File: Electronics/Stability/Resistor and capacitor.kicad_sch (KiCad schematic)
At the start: 5 parts, among them U1 ${SIM.PARAMS}

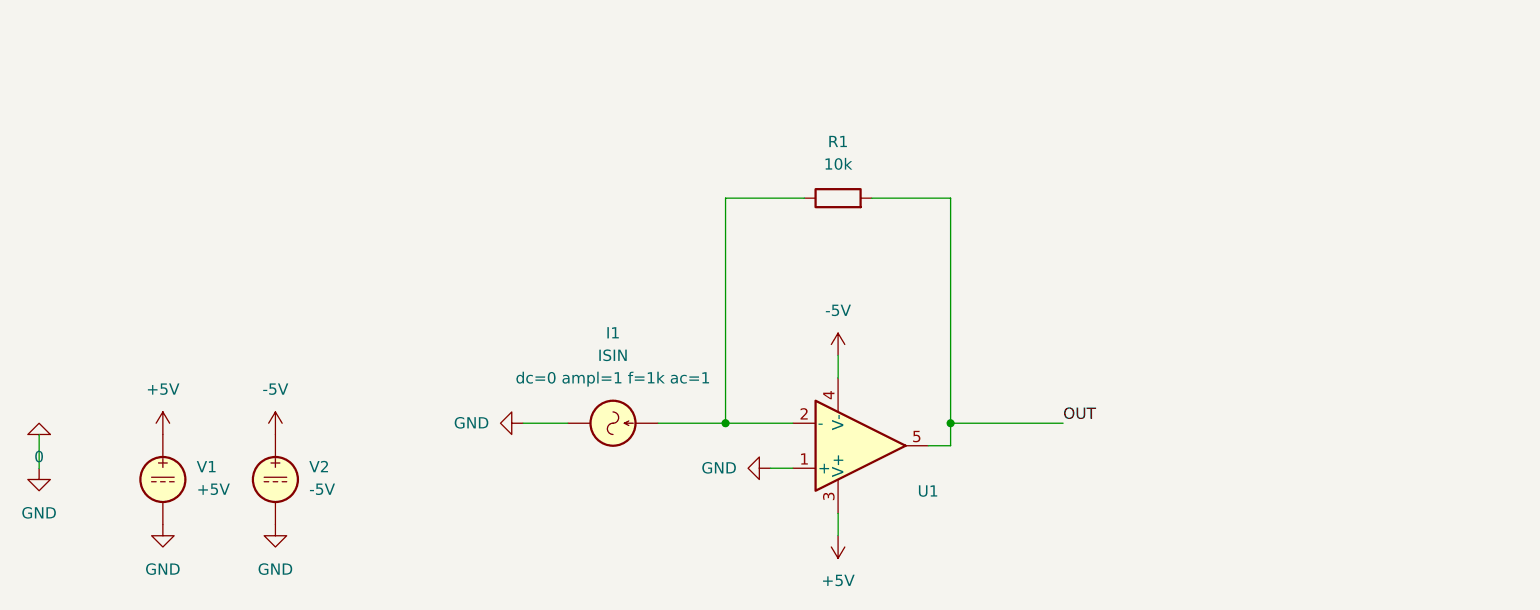
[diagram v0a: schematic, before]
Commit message: Create resistor + capacitor simulation
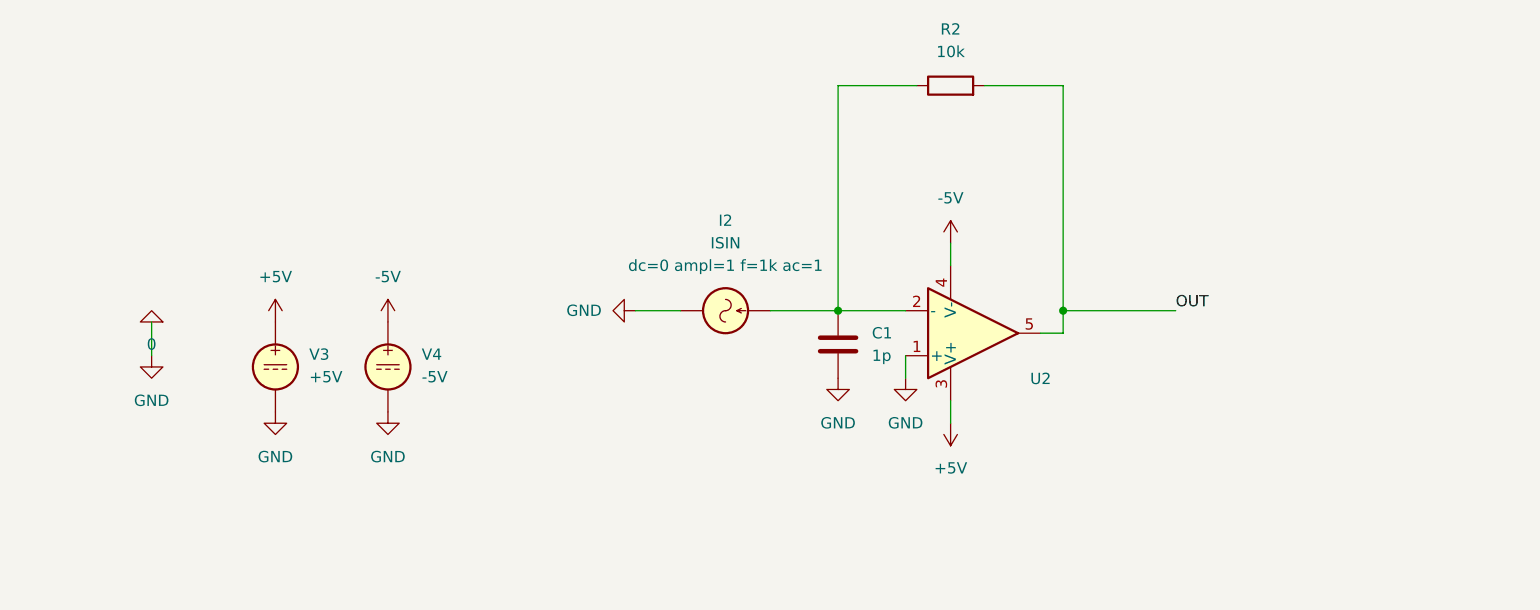
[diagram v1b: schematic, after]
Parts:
- removed I1: ISIN, symbol Simulation_SPICE:ISIN
- removed R1: 10k, symbol Device:R
- removed U1: ${SIM.PARAMS}, symbol Simulation_SPICE:OPAMP
- removed V1: +5V, symbol Simulation_SPICE:VDC
- removed V2: -5V, symbol Simulation_SPICE:VDC
- added C1: 1p, symbol Device:C
- added I2: ISIN, symbol Simulation_SPICE:ISIN
- added R2: 10k, symbol Device:R
- added U2: ${SIM.PARAMS}, symbol Simulation_SPICE:OPAMP
- added V3: +5V, symbol Simulation_SPICE:VDC
- added V4: -5V, symbol Simulation_SPICE:VDC
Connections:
- net +5V: now also U2.3 (V+), V3.1
- net -5V: now also U2.4 (V-), V4.1
- net 0: now also C1.2, I2.2, U2.1 (+), V3.2, V4.2
- net OUT: now also R2.2, U2.5
- new net: C1.1, I2.1, R2.1, U2.2 (-)

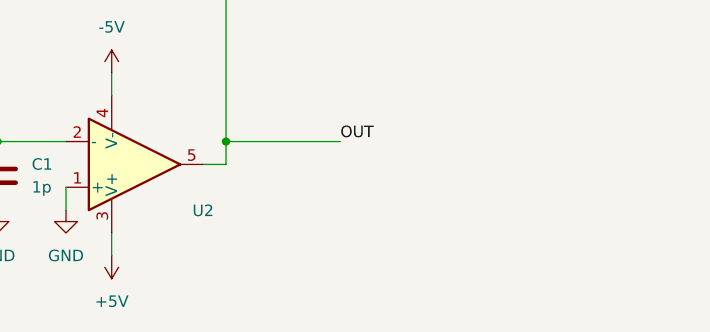
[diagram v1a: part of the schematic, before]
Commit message: Create stability compensation simulation
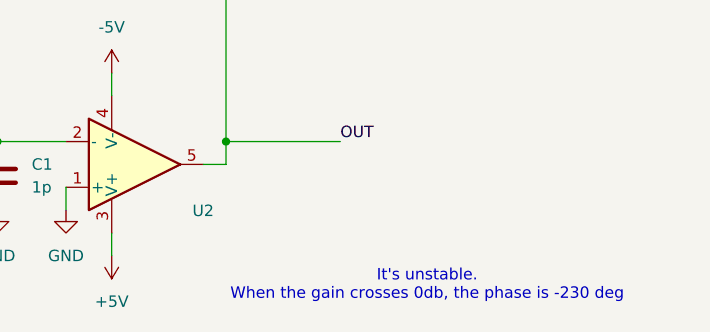
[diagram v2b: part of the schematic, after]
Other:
- note added: "It's unstable. When the gain crosses 0db, the phase is -230 deg"
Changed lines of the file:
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@@
 	(generator_version "10.0")
 	(paper "A4")
+	(text "It's unstable.\nWhen the gain crosses 0db, the phase is -230 deg"
+		(exclude_from_sim no)
+		(at 212.852 104.902 0)
+		(effects
+			(font
+				(size 1.27 1.27)
+			)
+		)
+	)
 	(junction
 		(at 190.5 88.9)
